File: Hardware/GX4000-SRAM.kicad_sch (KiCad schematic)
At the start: 7 parts, among them U1 IS62C1024AL-35QLI, U2 74HCT573, U3 74LVC1G32, U4 TMS4464, U5 TMS4464

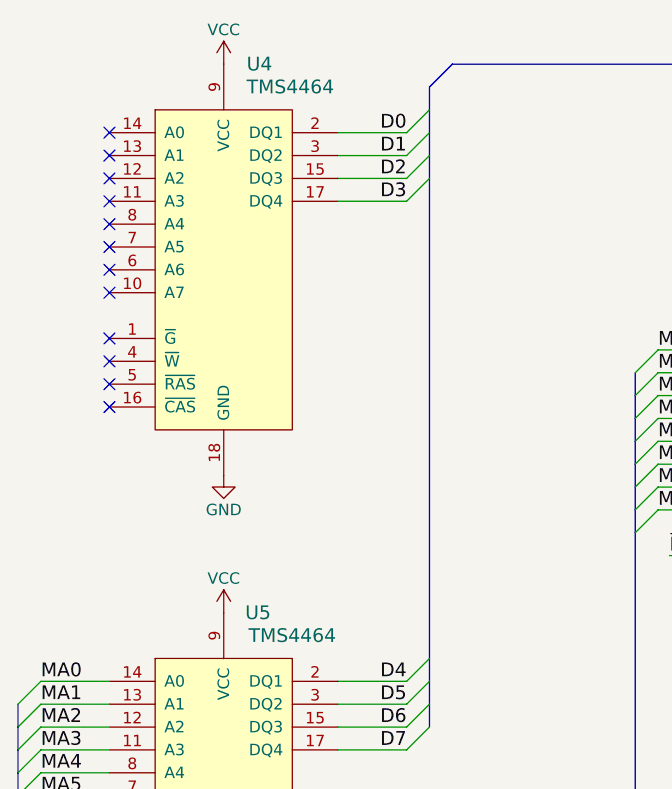
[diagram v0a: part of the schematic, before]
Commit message: Fixes the expacement between U10 and U11
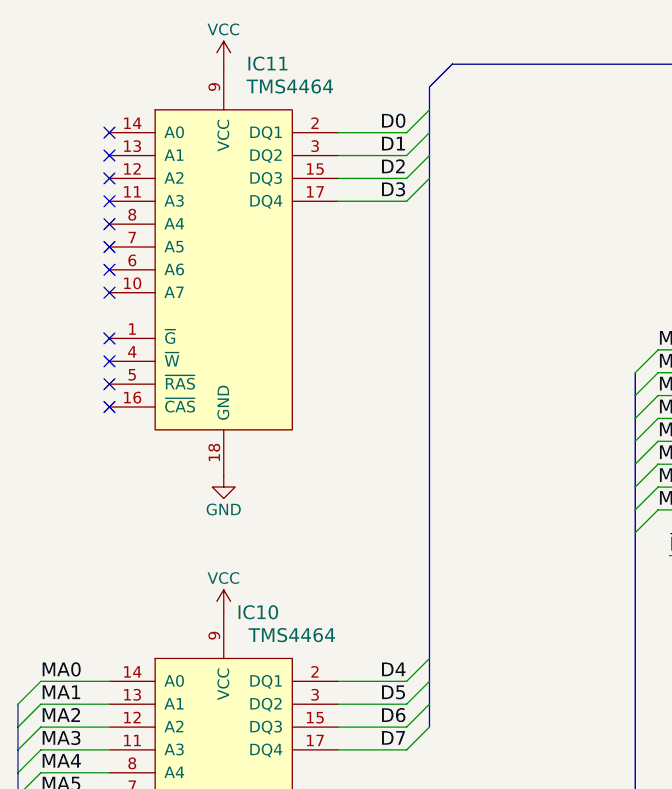
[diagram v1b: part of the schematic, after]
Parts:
- U3: footprint Package_SO:SO-6_4.4x3.6mm_P1.27mm -> Package_TO_SOT_SMD:SOT-23-5
- renumbered U5 to IC10, U4 to IC11
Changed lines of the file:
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@@
     (property "Reference" "U3" (id 0) (at 162.56 109.22 0))
     (property "Value" "74LVC1G32" (id 1) (at 166.37 111.76 0))
-    (property "Footprint" "Package_SO:SO-6_4.4x3.6mm_P1.27mm" (id 2) (at 158.75 116.84 0)
+    (property "Footprint" "Package_TO_SOT_SMD:SOT-23-5" (id 2) (at 158.75 116.84 0)
       (effects (font (size 1.27 1.27)) hide)
     )
@@
   (symbol (lib_name "TMS4464_1") (lib_id "c64-sram-rescue:TMS4464") (at 82.55 119.38 0) (unit 1)
     (in_bom yes) (on_board yes)
-    (property "Reference" "U5" (id 0) (at 86.36 97.79 0)
+    (property "Reference" "IC10" (id 0) (at 86.36 97.79 0)
       (effects (font (size 1.524 1.524)))
     )
@@
   (symbol (lib_id "Additionnal:TMS4464") (at 82.55 58.42 0) (unit 1)
     (in_bom yes) (on_board yes)
-    (property "Reference" "U4" (id 0) (at 85.09 36.83 0)
+    (property "Reference" "IC11" (id 0) (at 85.09 36.83 0)
       (effects (font (size 1.524 1.524)) (justify left))
     )
@@
       (reference "C2") (unit 1) (value "100nF") (footprint "Capacitor_SMD:C_0805_2012Metric")
     )
+    (path "/1fefcc37-fea1-407c-a9a6-08db0277cff7"
+      (reference "IC10") (unit 1) (value "TMS4464") (footprint "Package_DIP:DIP-18_W7.62mm_LongPads")
+    )
+    (path "/af651530-8916-4f71-9b0d-f7d4bdae3246"
+      (reference "IC11") (unit 1) (value "TMS4464") (footprint "Package_DIP:DIP-18_W7.62mm_LongPads")
+    )
     (path "/31d53c6d-e2a4-44c2-b22a-3991674b2b75"
       (reference "U1") (unit 1) (value "IS62C1024AL-35QLI") (footprint "Package_SO:SSOP-32_11.305x20.495mm_P1.27mm")
@@
     )
     (path "/071f3557-2171-44bb-8d22-fa7193123143"
-      (reference "U3") (unit 1) (value "74LVC1G32") (footprint "Package_SO:SO-6_4.4x3.6mm_P1.27mm")
-    )
-    (path "/af651530-8916-4f71-9b0d-f7d4bdae3246"
-      (reference "U4") (unit 1) (value "TMS4464") (footprint "Package_DIP:DIP-18_W7.62mm_LongPads")
-    )
-    (path "/1fefcc37-fea1-407c-a9a6-08db0277cff7"
-      (reference "U5") (unit 1) (value "TMS4464") (footprint "Package_DIP:DIP-18_W7.62mm_LongPads")
-    )
-  )
+      (reference "U3") (unit 1) (value "74LVC1G32") (footprint "Package_TO_SOT_SMD:SOT-23-5")
+    )
+  )

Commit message: Release PCB
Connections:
- net D0: now also IC10.2 (DQ1); no longer IC11.2 (DQ1)
- net D1: now also IC10.3 (DQ2); no longer IC11.3 (DQ2)
- net D2: now also IC10.15 (DQ3); no longer IC11.15 (DQ3)
- net D3: now also IC10.17 (DQ4); no longer IC11.17 (DQ4)
- net D4: now also IC11.2 (DQ1); no longer IC10.2 (DQ1)
- net D5: now also IC11.3 (DQ2); no longer IC10.3 (DQ2)
- net D6: now also IC11.15 (DQ3); no longer IC10.15 (DQ3)
- net D7: now also IC11.17 (DQ4); no longer IC10.17 (DQ4)
- net MA4: now also IC11.8 (A4); no longer IC10.8 (A4)
- net MA6: now also IC11.6 (A6); no longer IC10.6 (A6)
- net MA7: now also IC11.10 (A7); no longer IC10.10 (A7)
- net ~{CAS}: now also U3.1; no longer U3.2
- net ~{RAS}: now also U3.2; no longer U3.1
- net ~{WE}: now also IC11.4 (~{W}); no longer IC10.4 (~{W})

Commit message: v2.1
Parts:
- removed U1: IS62C1024AL-35QLI, Package_SO:SSOP-32_11.305x20.495mm_P1.27mm, symbol Additionnal:IS62C1024AL-35QLI
- added CAS1: Conn_01x01, Connector_Pin:Pin_D0.7mm_L6.5mm_W1.8mm_FlatFork, symbol Connector_Generic:Conn_01x01
- added R1: 47k, Resistor_SMD:R_0805_2012Metric, symbol Device:R
- added R2: 33, Resistor_SMD:R_0805_2012Metric, symbol Device:R
- added U1: IS61C1024AL-12HLI, Package_SO:TSOP-I-32_11.8x8mm_P0.5mm, symbol Additionnal:IS61C1024AL-12HLI
- added U4: 74LVC1G08, Package_TO_SOT_SMD:SOT-23-5, symbol 74xGxx:74LVC1G08
- IC10: footprint Package_DIP:DIP-18_W7.62mm_LongPads -> Housings_DIP:DIP-18_W7.62mm_LongPads; symbol c64-sram-rescue:TMS4464 -> Additionnal:TMS4464
- IC11: footprint Package_DIP:DIP-18_W7.62mm_LongPads -> Housings_DIP:DIP-18_W7.62mm_LongPads
- U2: value 74HCT573 -> SN74HCT573PWR; footprint Package_SO:SOP-20_7.5x12.8mm_P1.27mm -> Package_SO:TSSOP-20_4.4x6.5mm_P0.65mm
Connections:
- net A0: now also U2.15 (Q4), U1.20 (A0); no longer U2.19 (Q0)
- net A1: now also U2.14 (Q5), U1.19 (A1); no longer U2.18 (Q1)
- net A2: now also U2.13 (Q6), U1.18 (A2); no longer U2.17 (Q2)
- net A3: now also U2.12 (Q7), U1.17 (A3); no longer U2.16 (Q3)
- net A4: now also U2.16 (Q3), U1.16 (A4); no longer U2.15 (Q4)
- net A5: now also U2.17 (Q2), U1.15 (A5); no longer U2.14 (Q5)
- net A6: now also U2.18 (Q1), U1.14 (A6); no longer U2.13 (Q6)
- net A7: now also U2.19 (Q0), U1.13 (A7); no longer U2.12 (Q7)
- net D0: now also U1.21 (I/O0)
- net D1: now also U1.22 (I/O1)
- net D2: now also U1.23 (I/O2)
- net D3: now also U1.25 (I/O3)
- net D4: now also U1.26 (I/O4)
- net D5: now also U1.27 (I/O5)
- net D6: now also U1.28 (I/O6)
- net D7: now also U1.29 (I/O7)
- net GND: now also U1.24 (GND), U4.3 (GND)
- net MA0: now also IC11.14 (A0), U2.6 (D4), U1.3 (A8); no longer U2.2 (D0)
- net MA1: now also IC11.13 (A1), U2.7 (D5), U1.2 (A9); no longer U2.3 (D1)
- net MA2: now also IC11.12 (A2), U2.8 (D6), U1.31 (A10); no longer U2.4 (D2)
- net MA3: now also IC11.11 (A3), U2.9 (D7), U1.1 (A11); no longer U2.5 (D3)
- net MA4: now also IC10.8 (A4), U2.5 (D3), U1.12 (A12); no longer U2.6 (D4)
- net MA5: now also IC11.7 (A5), U2.4 (D2), U1.4 (A13); no longer U2.7 (D5)
- net MA6: now also IC10.6 (A6), U2.3 (D1), U1.11 (A14); no longer U2.8 (D6)
- net MA7: now also IC10.10 (A7), U2.2 (D0), U1.7 (A15); no longer U2.9 (D7)
- net VCC: now also R1.1, U1.6 (CE2), U1.8 (VDD), U4.5 (VCC)
- net ~{OE}: now also IC11.1 (~{G}), U1.32 (~{OE})
- net ~{RAS}: now also IC11.5 (~{RAS})
- net ~{WE}: now also IC10.4 (~{W}), U1.5 (~{WE})
- net at U3.4: now also U1.30 (~{CE1})
- net ~{CAS0}: now reaches IC11.16 (~{CAS})
- net ~{CAS0}: now also IC10.16 (~{CAS}), U1.10 (A16), U4.2
- net ~{CAS}: no longer names the net of U3.1
- net ~{CAS}: now also U4.4; no longer IC10.16 (~{CAS})
- new net: CAS1.1 (Pin_1), R2.1
- new net ~{CAS1}: R1.2, R2.2, U4.1
- no-connect marks 12 -> 0
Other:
- title: GX4000-SRAM -> GX4000-SRAM-128K
- moved on the sheet: IC10, IC11, U2, U3
